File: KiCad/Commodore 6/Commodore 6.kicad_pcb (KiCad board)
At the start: 2 copper layers, 0 parts

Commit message: Update Commodore 6.kicad_pcb
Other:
- board outline added: 127 x 127 mm
- copper layers 2 -> 4
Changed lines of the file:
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@@
 	(layers
 		(0 "F.Cu" signal)
+		(4 "In1.Cu" signal)
+		(6 "In2.Cu" signal)
 		(2 "B.Cu" signal)
 		(9 "F.Adhes" user "F.Adhesive")
@@
 			)
 			(layer "dielectric 1"
+				(type "prepreg")
+				(thickness 0.1)
+				(material "FR4")
+				(epsilon_r 4.5)
+				(loss_tangent 0.02)
+			)
+			(layer "In1.Cu"
+				(type "copper")
+				(thickness 0.035)
+			)
+			(layer "dielectric 2"
 				(type "core")
-				(thickness 1.51)
+				(thickness 1.24)
+				(material "FR4")
+				(epsilon_r 4.5)
+				(loss_tangent 0.02)
+			)
+			(layer "In2.Cu"
+				(type "copper")
+				(thickness 0.035)
+			)
+			(layer "dielectric 3"
+				(type "prepreg")
+				(thickness 0.1)
 				(material "FR4")
 				(epsilon_r 4.5)
@@
 	)
 	(net 0 "")
+	(gr_rect
+		(start 78.9 30.3)
+		(end 205.9 157.3)
+		(stroke
+			(width 0.5)
+			(type solid)
+		)
+		(fill no)
+		(layer "Edge.Cuts")
+	)
 	(embedded_fonts no)
 )

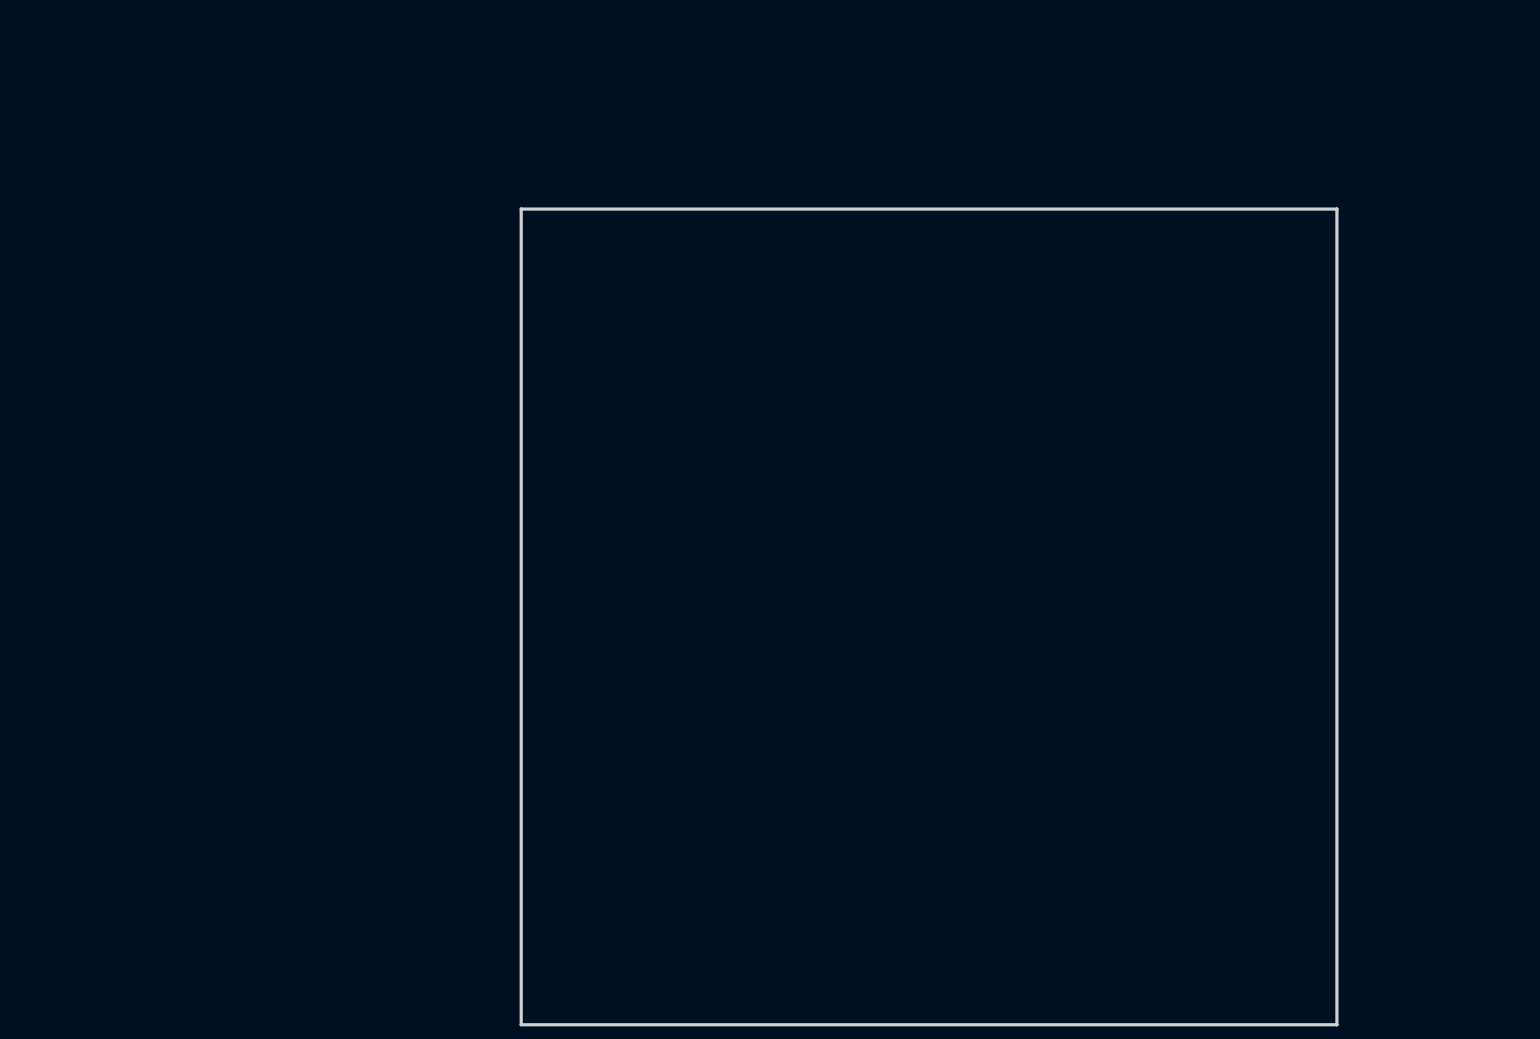
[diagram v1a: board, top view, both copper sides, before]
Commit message: Added most footprints
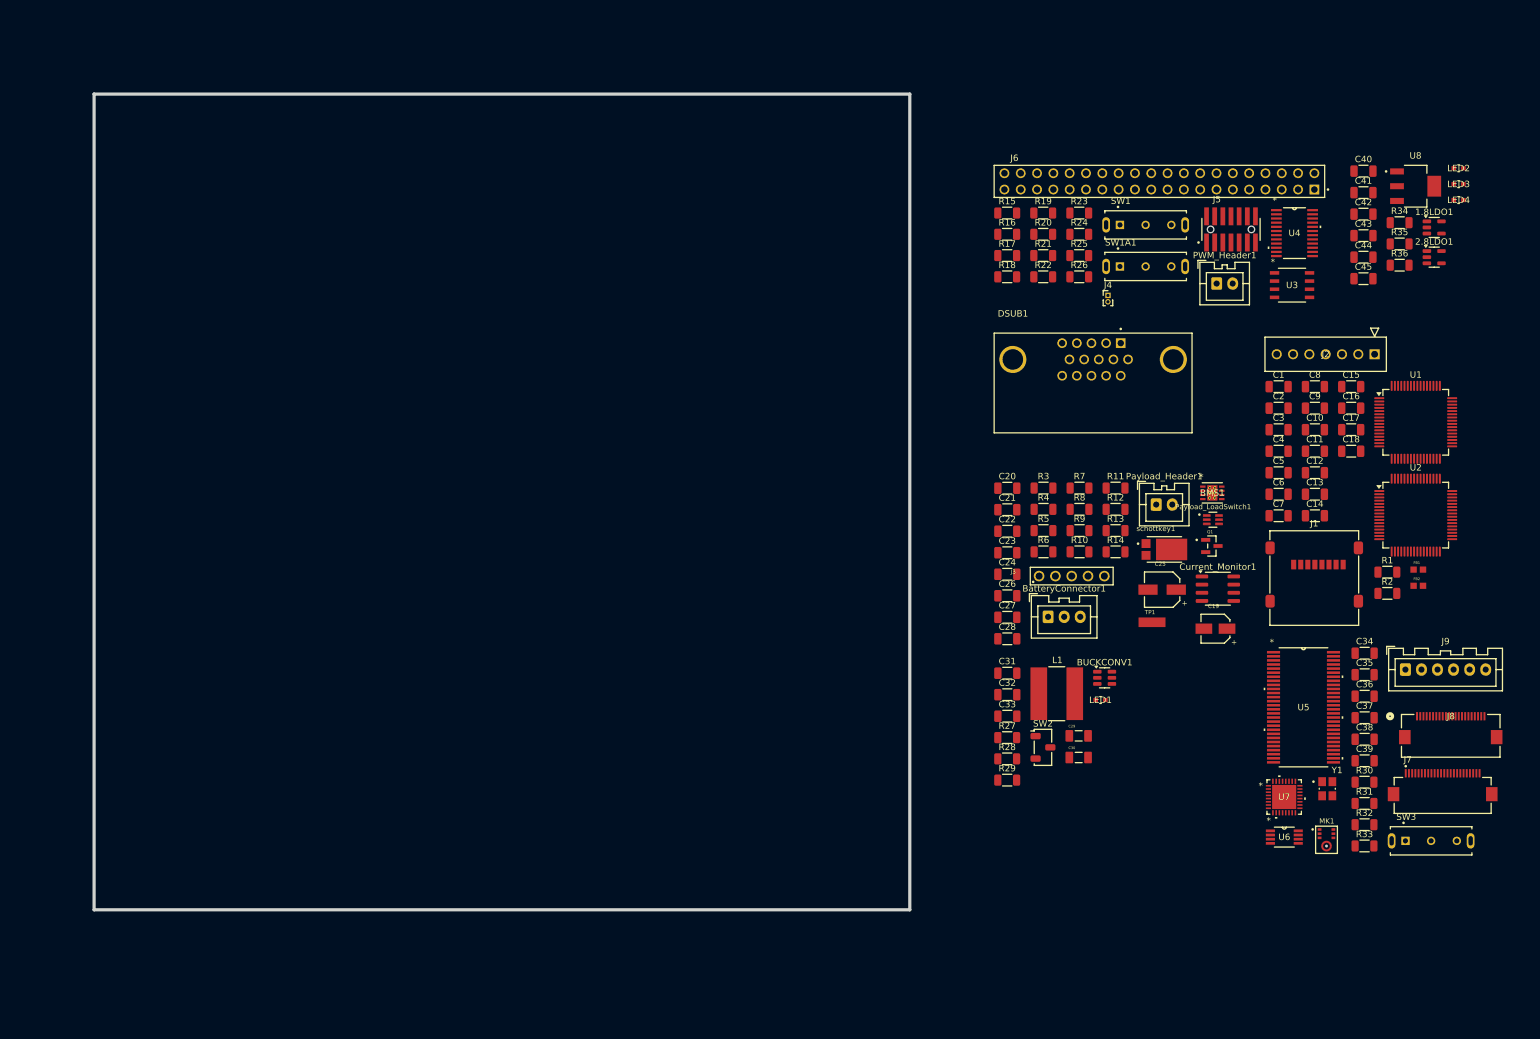
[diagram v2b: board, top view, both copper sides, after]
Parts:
- added 1.8LDO1: LP5907MFX-1.8, Package_TO_SOT_SMD:SOT-23-5, F.Cu at (221.0, 33.2)
- added 2.8LDO1: LP5907MFX-2.8, Package_TO_SOT_SMD:SOT-23-5, F.Cu at (221.0, 37.8)
- added BMS1: BQ29209DRBR, BQ29209DRBR Protection IC:DRB8_1P6X2P4, F.Cu at (186.5, 74.5)
- added BUCKCONV1: TPS563200, Package_TO_SOT_SMD:SOT-23-6, F.Cu at (169.7, 103.3)
- added BatteryConnector1: B03B-XASK-1, Connector_JST:JST_XA_B03B-XASK-1_1x03_P2.50mm_Vertical, F.Cu at (160.9, 93.8)
- added C1: 10uF, Capacitor_SMD:C_1206_3216Metric, F.Cu at (196.8, 58.0)
- added C10: 10uF, Capacitor_SMD:C_1206_3216Metric, F.Cu at (202.5, 64.7)
- added C11: 100nF, Capacitor_SMD:C_1206_3216Metric, F.Cu at (202.5, 68.0)
- added C12: 100nF, Capacitor_SMD:C_1206_3216Metric, F.Cu at (202.5, 71.3)
- added C13: 100nF, Capacitor_SMD:C_1206_3216Metric, F.Cu at (202.5, 74.7)
- added C14: 100nF, Capacitor_SMD:C_1206_3216Metric, F.Cu at (202.5, 78.0)
- added C15: 100nF, Capacitor_SMD:C_1206_3216Metric, F.Cu at (208.1, 58.0)
- added C16: 10nF, Capacitor_SMD:C_1206_3216Metric, F.Cu at (208.1, 61.3)
- added C17: 1uF, Capacitor_SMD:C_1206_3216Metric, F.Cu at (208.1, 64.7)
- added C18: 1uF, Capacitor_SMD:C_1206_3216Metric, F.Cu at (208.1, 68.0)
- added C19: WCAP-ASLL_4X5.5/865060640001 1uf smd electrolytic, 865060640001 1uf electrolytic:WCAP-ASLL_4X5.5_DXL_, F.Cu at (187.0, 95.6)
- added C2: 100nF, Capacitor_SMD:C_1206_3216Metric, F.Cu at (196.8, 61.3)
- added C20: 0.1uF, Capacitor_SMD:C_1206_3216Metric, F.Cu at (154.6, 73.8)
- added C21: 0.1uF, Capacitor_SMD:C_1206_3216Metric, F.Cu at (154.6, 77.1)
- added C22: 10uF, Capacitor_SMD:C_1206_3216Metric, F.Cu at (154.6, 80.5)
- added C23: 0.33uF, Capacitor_SMD:C_1206_3216Metric, F.Cu at (154.6, 83.8)
- added C24: 0.1uF, Capacitor_SMD:C_1206_3216Metric, F.Cu at (154.6, 87.2)
- added C25: WCAP-ASLI_5X5.5/ 47uf electro, 865080342006 47uf electrolytic:WCAP-ASLI_5X5.5_DXL_, F.Cu at (178.7, 89.6)
- added C26: 0.1uF, Capacitor_SMD:C_1206_3216Metric, F.Cu at (154.6, 90.5)
- added C27: 0.1uF, Capacitor_SMD:C_1206_3216Metric, F.Cu at (154.6, 93.9)
- added C28: 0.1uF, Capacitor_SMD:C_1206_3216Metric, F.Cu at (154.6, 97.2)
- added C29: CL31B106KAHNNNE/10uf, CL31B106KAHNNNE capacitor:CAPC3216X180N, F.Cu at (165.7, 112.3)
- added C3: 100nF, Capacitor_SMD:C_1206_3216Metric, F.Cu at (196.8, 64.7)
- added C30: CL31B106KAHNNNE/10uf, CL31B106KAHNNNE capacitor:CAPC3216X180N, F.Cu at (165.7, 115.7)
- added C31: 08053C104KAT2A/0.1uf, Capacitor_SMD:C_1206_3216Metric, F.Cu at (154.6, 102.6)
- added C32: CL10A226MP8NUNE/22uf, Capacitor_SMD:C_1206_3216Metric, F.Cu at (154.6, 105.9)
- added C33: CL10A226MP8NUNE/22uf, Capacitor_SMD:C_1206_3216Metric, F.Cu at (154.6, 109.3)
- added C34: 20nF, Capacitor_SMD:C_1206_3216Metric, F.Cu at (210.2, 99.5)
- added C35: 20nF, Capacitor_SMD:C_1206_3216Metric, F.Cu at (210.2, 102.8)
- added C36: 0.1uF, Capacitor_SMD:C_1206_3216Metric, F.Cu at (210.2, 106.2)
- added C37: 0.1uF, Capacitor_SMD:C_1206_3216Metric, F.Cu at (210.2, 109.5)
- added C38: 0.1uF, Capacitor_SMD:C_1206_3216Metric, F.Cu at (210.2, 112.8)
- added C39: 0.1uF, Capacitor_SMD:C_1206_3216Metric, F.Cu at (210.2, 116.2)
- added C4: 100nF, Capacitor_SMD:C_1206_3216Metric, F.Cu at (196.8, 68.0)
- added C40: CL10B105KP8NNNC 1uf, Capacitor_SMD:C_1206_3216Metric, F.Cu at (210.0, 24.4)
- added C41: CL10B105KP8NNNC 1uf, Capacitor_SMD:C_1206_3216Metric, F.Cu at (210.0, 27.7)
- added C42: CL10B105KP8NNNC 1uf, Capacitor_SMD:C_1206_3216Metric, F.Cu at (210.0, 31.1)
- added C43: CL10B105KP8NNNC 1uf, Capacitor_SMD:C_1206_3216Metric, F.Cu at (210.0, 34.4)
- added C44: CL10B105KP8NNNC 1uf, Capacitor_SMD:C_1206_3216Metric, F.Cu at (210.0, 37.8)
- added C45: CL10B105KP8NNNC 1uf, Capacitor_SMD:C_1206_3216Metric, F.Cu at (210.0, 41.1)
- added C5: 100nF, Capacitor_SMD:C_1206_3216Metric, F.Cu at (196.8, 71.3)
- added C6: 100nF, Capacitor_SMD:C_1206_3216Metric, F.Cu at (196.8, 74.7)
- added C7: 10nF, Capacitor_SMD:C_1206_3216Metric, F.Cu at (196.8, 78.0)
- added C8: 1uF, Capacitor_SMD:C_1206_3216Metric, F.Cu at (202.5, 58.0)
- added C9: 1uF, Capacitor_SMD:C_1206_3216Metric, F.Cu at (202.5, 61.3)
- added Current_Monitor1: INA219AxD, Package_SO:SOIC-8_3.9x4.9mm_P1.27mm, F.Cu at (187.4, 89.4)
- added DSUB1: ICD15S13E4GX00LF, ICD15S13E4GX00LF dsub:AMPHENOL_ICD15S13E4GX00LF, F.Cu at (167.9, 53.7)
- added FB1: BLM18KG121TN1D, BLM18KG121TN1D STM Ferrite:BEADC1608X75N, F.Cu at (218.6, 86.4)
- added FB2: BLM18KG121TN1D, BLM18KG121TN1D STM Ferrite:BEADC1608X75N, F.Cu at (218.6, 89.0)
- added J1: 472192001, Connector_Card:microSD_HC_Molex_47219-2001, F.Cu at (202.4, 87.8)
- added J2: PPTC071LFBN-RC, PPTC071LFBN_RC 1x7 Header:CONN_xPxC071LFBN-RC_SUL, F.Cu at (211.8, 52.9)
- added J3: 6130XX11121_61300511121, 61300511121 5pin header:61300511121, F.Cu at (164.6, 87.4)
- added J4: Conn_01x02_Pin, Connector_PinHeader_1.00mm:PinHeader_1x02_P1.00mm_Vertical, F.Cu at (170.3, 43.7)
- added J5: FTSH-107-01-L-DV-K-A, FTSH_107_01_L_DV_K_A SWD Connecter:SAMTEC_FTSH-107-01-L-DV-K-A, F.Cu at (189.4, 33.5)
- added J6: M20-6112045, M20_6112045_40Pin_Header:HARWIN_M20-6112045, F.Cu at (178.3, 26.0)
- added J7: FH12-24S-0.5SH_55_, FH12_24S_0_5SH_55 Camera Connector:HRS_FH12-24S-0.5SH_55_, F.Cu at (222.4, 120.9)
- added J8: FH12-22S-0.5SH55, FH12_22S_0_5SH_55 C2I Camera Connector:CONN_FH12-22S-0.5SH55_HIR, F.Cu at (223.6, 112.3)
- added J9: Conn_01x06, Connector_JST:JST_XA_B06B-XASK-1_1x06_P2.50mm_Vertical, F.Cu at (216.6, 102.0)
- added L1: SRN8040-3R3Y/3.3uH, Inductor_SMD:L_Bourns-SRN8040_8x8.15mm, F.Cu at (162.3, 105.8)
- added LED1: LTST-C190KRKT, LTST_C190KRKT red led:LED_LTST-C190_LTO, F.Cu at (169.1, 106.7)
- added LED2: LTST-C190KRKT, LTST_C190KRKT red led:LED_LTST-C190_LTO, F.Cu at (224.8, 24.0)
- added LED3: LTST-C190KRKT, LTST_C190KRKT red led:LED_LTST-C190_LTO, F.Cu at (224.8, 26.4)
- added LED4: LTST-C190KRKT, LTST_C190KRKT red led:LED_LTST-C190_LTO, F.Cu at (224.8, 28.9)
- added MK1: DMM-4026-B-I2S-R, DMM_4026_B_I2S_R Microphone:MIC_DMM-4026-B-I2S-R, F.Cu at (204.3, 128.5)
- added PWM_Header1: B02B-XASK-1LFSN, Connector_JST:JST_XA_B02B-XASK-1_1x02_P2.50mm_Vertical, F.Cu at (187.2, 41.9)
- added Payload_Header1: B02B-XASK-1LFSN, Connector_JST:JST_XA_B02B-XASK-1_1x02_P2.50mm_Vertical, F.Cu at (177.8, 76.3)
- added Payload_LoadSwitch1: TPS22919DCKR, TPS22919DCKR:SOT65P210X110-6N, F.Cu at (186.6, 78.7)
- added Q1: NTR4501NT1G, NTR4501NT1G:SOT95P237X111-3N, F.Cu at (186.4, 82.8)
- added R1: 20K, Resistor_SMD:R_1206_3216Metric, F.Cu at (213.8, 86.8)
- added R10: RC0402JR-071KL 1k, Resistor_SMD:R_1206_3216Metric, F.Cu at (165.8, 83.7)
- added R11: 100, Resistor_SMD:R_1206_3216Metric, F.Cu at (171.4, 73.7)
- added R12: 1k, Resistor_SMD:R_1206_3216Metric, F.Cu at (171.4, 77.0)
- added R13: 470k, Resistor_SMD:R_1206_3216Metric, F.Cu at (171.4, 80.4)
- added R14: 330k, Resistor_SMD:R_1206_3216Metric, F.Cu at (171.4, 83.7)
- added R15: 100R, Resistor_SMD:R_1206_3216Metric, F.Cu at (154.6, 30.9)
- added R16: 120R, Resistor_SMD:R_1206_3216Metric, F.Cu at (154.6, 34.2)
- added R17: 120R, Resistor_SMD:R_1206_3216Metric, F.Cu at (154.6, 37.5)
- added R18: 50R, Resistor_SMD:R_1206_3216Metric, F.Cu at (154.6, 40.9)
- added R19: 100K, Resistor_SMD:R_1206_3216Metric, F.Cu at (160.2, 30.9)
- added R2: 20K, Resistor_SMD:R_1206_3216Metric, F.Cu at (213.8, 90.1)
- added R20: 100K, Resistor_SMD:R_1206_3216Metric, F.Cu at (160.2, 34.2)
- added R21: 50R, Resistor_SMD:R_1206_3216Metric, F.Cu at (160.2, 37.5)
- added R22: 50R, Resistor_SMD:R_1206_3216Metric, F.Cu at (160.2, 40.9)
- added R23: 50R, Resistor_SMD:R_1206_3216Metric, F.Cu at (165.8, 30.9)
- added R24: 100K, Resistor_SMD:R_1206_3216Metric, F.Cu at (165.8, 34.2)
- added R25: 50R, Resistor_SMD:R_1206_3216Metric, F.Cu at (165.8, 37.5)
- added R26: 50R, Resistor_SMD:R_1206_3216Metric, F.Cu at (165.8, 40.9)
- added R27: RC0201FR-0756K2L/56.2K ohm, Resistor_SMD:R_1206_3216Metric, F.Cu at (154.6, 112.6)
- added R28: RC0201FR-0710KL/10kohm, Resistor_SMD:R_1206_3216Metric, F.Cu at (154.6, 115.9)
- added R29: RC1206FR-07249RL/220ohm, Resistor_SMD:R_1206_3216Metric, F.Cu at (154.6, 119.2)
- added R3: ERA-3VRW6801V 6.8k ohm, Resistor_SMD:R_1206_3216Metric, F.Cu at (160.2, 73.7)
- added R30: 10K, Resistor_SMD:R_1206_3216Metric, F.Cu at (210.2, 119.5)
- added R31: 10K, Resistor_SMD:R_1206_3216Metric, F.Cu at (210.2, 122.8)
- added R32: 750R, Resistor_SMD:R_1206_3216Metric, F.Cu at (210.2, 126.2)
- added R33: 10K, Resistor_SMD:R_1206_3216Metric, F.Cu at (210.2, 129.5)
- added R34: RC0805FR-07150RL, Resistor_SMD:R_1206_3216Metric, F.Cu at (215.7, 32.4)
- added R35: ERJ-2RKF1000X, Resistor_SMD:R_1206_3216Metric, F.Cu at (215.7, 35.7)
- added R36: RC0805FR-07150RL, Resistor_SMD:R_1206_3216Metric, F.Cu at (215.7, 39.0)
- added R4: ERA-3VRW3301V 3.3k ohm, Resistor_SMD:R_1206_3216Metric, F.Cu at (160.2, 77.0)
- added R5: RC0201FR-0710KL/ 10k, Resistor_SMD:R_1206_3216Metric, F.Cu at (160.2, 80.4)
- added R6: 160, Resistor_SMD:R_1206_3216Metric, F.Cu at (160.2, 83.7)
- added R7: 260, Resistor_SMD:R_1206_3216Metric, F.Cu at (165.8, 73.7)
- added R8: 100, Resistor_SMD:R_1206_3216Metric, F.Cu at (165.8, 77.0)
- added R9: 2m, Resistor_SMD:R_1206_3216Metric, F.Cu at (165.8, 80.4)
- added SW1: SLW-1277744-3A-N-D, SLW_1277744_3A_N_D Switch:SW_SLW-1277744-3A-N-D, F.Cu at (176.1, 32.8)
- added SW1A1: SLW-1277744-3A-N-D, SLW_1277744_3A_N_D Switch:SW_SLW-1277744-3A-N-D, F.Cu at (176.1, 39.2)
- added SW2: SLW-1277744-3A-N-D, Button_Switch_SMD:Nidec_Copal_CAS-120A, F.Cu at (160.1, 114.1)
- added SW3: SLW-1277744-3A-N-D, SLW_1277744_3A_N_D Switch:SW_SLW-1277744-3A-N-D, F.Cu at (220.6, 128.7)
- added TP1: RCWCTE, RCWCTE testpoint:TP420X150, F.Cu at (177.1, 94.6)
- added U1: STM32H562RIT6, Package_QFP:LQFP-64_10x10mm_P0.5mm, F.Cu at (218.2, 63.5)
- added U2: STM32H7A3RIT6, Package_QFP:LQFP-64_10x10mm_P0.5mm, F.Cu at (218.2, 78.0)
- added U3: SN65HVD74DR, SN65HVD74DR Transceiver:D8_TEX, F.Cu at (198.9, 42.1)
- added U4: TS3A27518EIPWRQ1, TS3A27518EIPWRQ1 Demultiplexer:PW24, F.Cu at (199.3, 34.0)
- added U5: SN74CBT16233DLR, SN74CBT16233DLR Multiplexer:DL56, F.Cu at (200.7, 107.9)
- added U6: TCA9509DGKR, TCA9509DGKR Level Shifter:DGK8, F.Cu at (197.7, 128.1)
- added U7: ADV7280AWBCPZ, ADV7280AWBCPZ NTSC:CP-32-12_ADI, F.Cu at (197.7, 121.8)
- added U8: TLV1117LV33DCYR, TLV1117LV33DCYR 3.3 ldo:VREG_TLV1117LV33DCYR, F.Cu at (218.2, 26.7)
- added Y1: ABM8AIG-28.63636MHZ, ABM8AIG_28_63636MHZ_12_2Z_T3 Crystal:XTAL_ABM8AIG-28.63636MHZ-12-2Z-T3, F.Cu at (204.4, 120.5)
- added schottkey1: PDS1040L-13, PDS1040L_13 schottkey:DIO_PDS1040L-13, F.Cu at (179.0, 83.3)

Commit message: Can start Routing
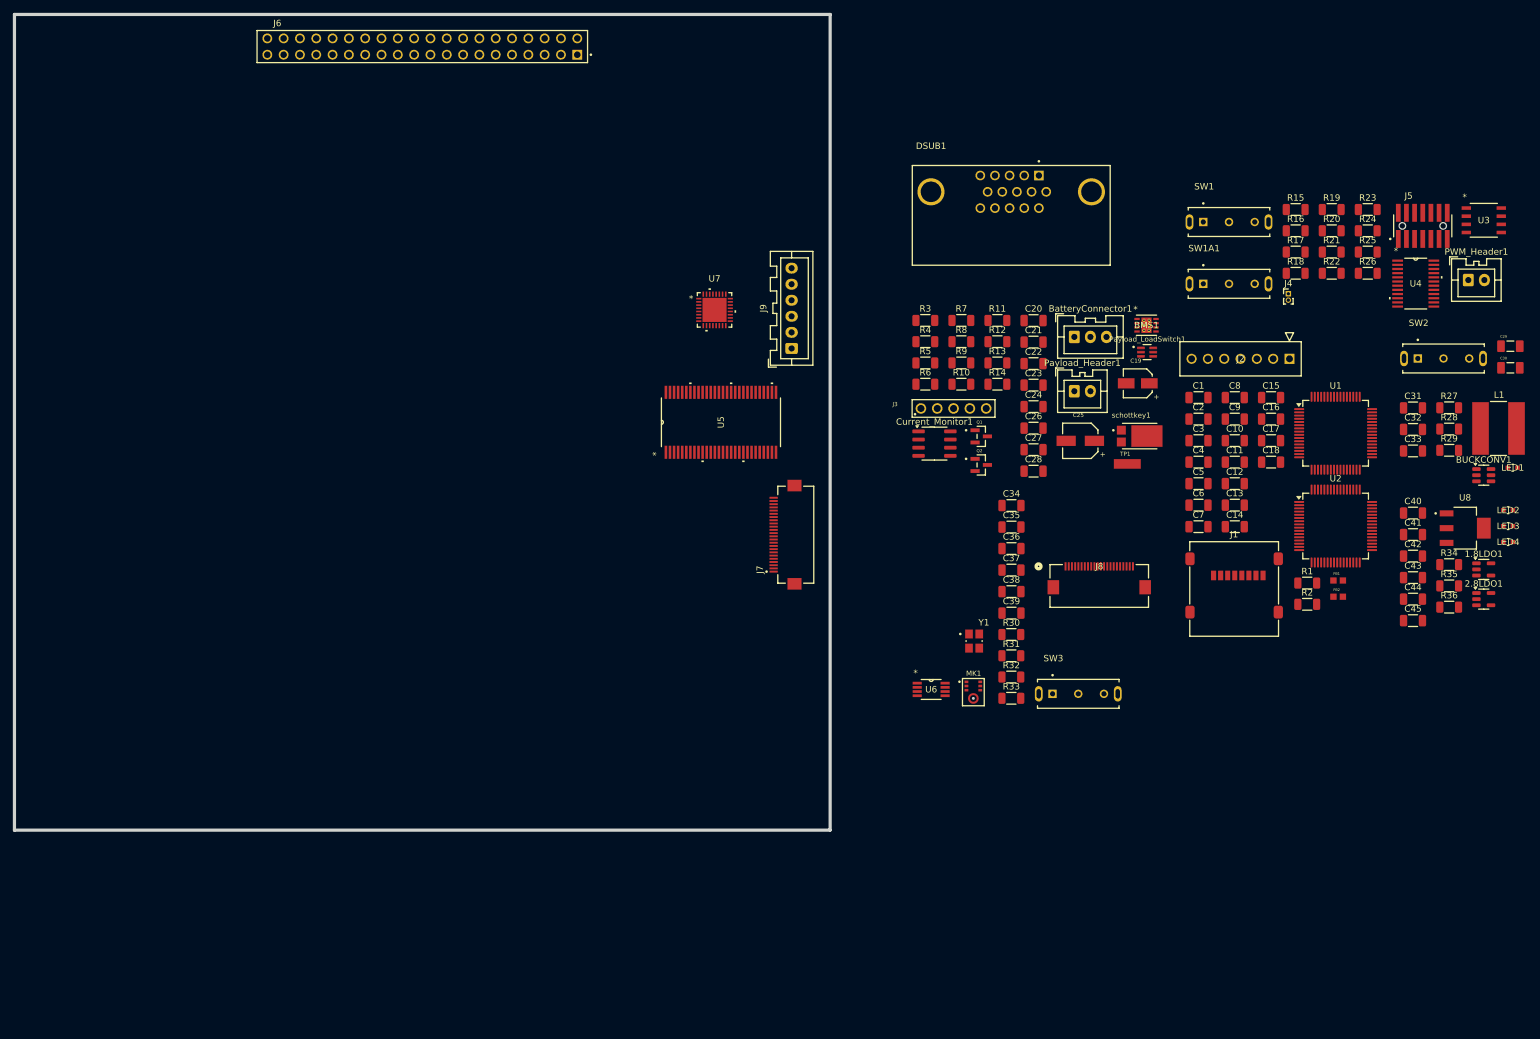
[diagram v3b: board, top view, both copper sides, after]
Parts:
- added Q2: PMOS, NTR4501NT1G:SOT95P237X111-3N, F.Cu at (150.5, 70.1)
- R27: value RC0201FR-0756K2L/56.2K ohm -> RC1206FR-07249RL/220ohm
- R28: value RC0201FR-0710KL/10kohm -> RC0201FR-0756K2L/56.2K ohm
- R29: value RC1206FR-07249RL/220ohm -> RC0201FR-0710KL/10kohm
- SW1, SW1A1, SW3: value SLW-1277744-3A-N-D -> SLW-1277545-3A-RA-N-D; footprint SLW_1277744_3A_N_D Switch:SW_SLW-1277744-3A-N-D -> SLW_1277545_3A_RA_N_D HSwitch:SW_SLW-1277545-3A-RA-N-D
- SW2: value SLW-1277744-3A-N-D -> SLW-1277545-3A-RA-N-D; footprint Button_Switch_SMD:Nidec_Copal_CAS-120A -> SLW_1277545_3A_RA_N_D HSwitch:SW_SLW-1277545-3A-RA-N-D
- moved U7 116.7 mm to (109.0, 46.0)
- moved J6 116.7 mm to (63.5, 5.00)
- moved J7 109.0 mm to (121.0, 81.0), turned to 90 degrees
- moved J9 107.9 mm to (121.0, 52.0), turned to 90 degrees
- moved U5 101.0 mm to (110.0, 63.5), turned to 90 degrees
- moved C29 90.5 mm to (232.9, 51.6)
- moved C30 90.5 mm to (232.9, 55.0)
- moved SW2 86.9 mm to (222.5, 53.6)
- moved R27 85.9 mm to (223.4, 61.2)
- moved R28 85.9 mm to (223.4, 64.5)
- moved R29 85.9 mm to (223.4, 67.9)
- moved L1 80.2 mm to (231.1, 64.5)
- moved C33 75.5 mm to (217.8, 68.0)
- moved C31 75.5 mm to (217.8, 61.3)
- moved C32 75.5 mm to (217.8, 64.6)
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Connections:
- R27 pad 1: Net-(BUCKCONV1-VFB) -> Net-(LED1-Pad2)
- R28 pad 1: GNDA -> Net-(BUCKCONV1-VFB)
- R28 pad 2: Net-(BUCKCONV1-VFB) -> 5V
- R29 pad 1: Net-(LED1-Pad2) -> GNDA
- R29 pad 2: 5V -> Net-(BUCKCONV1-VFB)
